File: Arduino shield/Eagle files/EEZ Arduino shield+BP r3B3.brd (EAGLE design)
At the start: 207 x 74 mm, 181 parts, among them IC1 TLC5925IDBQR, IC10 BC857BS, IC11 TLC555, IC12 SN74LVC2G08DCTR, IC13 TPS3705-33D, IC14 SN74LV1T34DBVR, IC15 SN74LVC2G02DCTR, IC2 Si8641EC-B-IS1, IC3 SI8651EC-B-IS1, IC4 SI8651EC-B-IS1, IC5 LD1117ADT33TR, IC6 Si8641EC-B-IS1, IC7 PCA21125, IC8 AT25256B, IC9 W5500, J1 BS-244DSM-R, J2 BS-244DSM-G, J3 BS-244DSM-B, J4 BS-244DSM-R, J5 BS-244DSM-B, Q1 IRLML2246TRPBF, Q2 IRLML2246TRPBF, Q3 IRLML2246TRPBF, Q4 IRLML2246TRPBF, Q5 2N7002, Q6 IRLML2246TRPBF, Q7 2N7002, Q8 2N7002, SW1 A101SYCQ04, SW2 1301.9316, X1 MC000006, X2 TSW-113-07-F-D, X3 MC000005, X4 TSW-113-07-F-D, X5 09185067324, X6 22-23-2021, X7 826629-8, X8 22-23-2041, X9 SSW-105-02-S-D, Y1 32,768kHz, Y2 25MHz

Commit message: Arduino Shield correction
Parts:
- C28, C32: device rcl:C0603 -> rcl:C0805
- moved C28 0.32 mm to (134.7, 21.9)
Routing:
- net CH1_VDD: vias 10 -> 9
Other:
- board text added: "1"
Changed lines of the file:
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@@
 <grid distance="2.5" unitdist="mil" unit="mil" style="lines" multiple="10" display="no" altdistance="5" altunitdist="mm" altunit="mm"/>
 <layers>
-<layer number="1" name="Top" color="4" fill="1" visible="no" active="yes"/>
+<layer number="1" name="Top" color="4" fill="1" visible="yes" active="yes"/>
 <layer number="2" name="Route2" color="1" fill="3" visible="no" active="no"/>
 <layer number="3" name="Route3" color="4" fill="3" visible="no" active="no"/>
@@
 <layer number="14" name="Route14" color="1" fill="6" visible="no" active="no"/>
 <layer number="15" name="Route15" color="4" fill="6" visible="no" active="no"/>
-<layer number="16" name="Bottom" color="1" fill="1" visible="no" active="yes"/>
-<layer number="17" name="Pads" color="14" fill="1" visible="no" active="yes"/>
-<layer number="18" name="Vias" color="14" fill="1" visible="no" active="yes"/>
-<layer number="19" name="Unrouted" color="6" fill="1" visible="no" active="yes"/>
-<layer number="20" name="Dimension" color="15" fill="1" visible="no" active="yes"/>
-<layer number="21" name="tPlace" color="7" fill="1" visible="no" active="yes"/>
-<layer number="22" name="bPlace" color="13" fill="1" visible="yes" active="yes"/>
-<layer number="23" name="tOrigins" color="15" fill="1" visible="no" active="yes"/>
+<layer number="16" name="Bottom" color="1" fill="1" visible="yes" active="yes"/>
+<layer number="17" name="Pads" color="14" fill="1" visible="yes" active="yes"/>
+<layer number="18" name="Vias" color="14" fill="1" visible="yes" active="yes"/>
+<layer number="19" name="Unrouted" color="6" fill="1" visible="yes" active="yes"/>
+<layer number="20" name="Dimension" color="15" fill="1" visible="yes" active="yes"/>
+<layer number="21" name="tPlace" color="7" fill="1" visible="yes" active="yes"/>
+<layer number="22" name="bPlace" color="13" fill="1" visible="no" active="yes"/>
+<layer number="23" name="tOrigins" color="15" fill="1" visible="yes" active="yes"/>
 <layer number="24" name="bOrigins" color="15" fill="1" visible="no" active="yes"/>
-<layer number="25" name="tNames" color="7" fill="1" visible="no" active="yes"/>
-<layer number="26" name="bNames" color="5" fill="1" visible="yes" active="yes"/>
+<layer number="25" name="tNames" color="7" fill="1" visible="yes" active="yes"/>
+<layer number="26" name="bNames" color="5" fill="1" visible="no" active="yes"/>
 <layer number="27" name="tValues" color="10" fill="1" visible="no" active="yes"/>
 <layer number="28" name="bValues" color="14" fill="1" visible="no" active="yes"/>
-<layer number="29" name="tStop" color="7" fill="3" visible="no" active="yes"/>
+<layer number="29" name="tStop" color="7" fill="3" visible="yes" active="yes"/>
 <layer number="30" name="bStop" color="7" fill="6" visible="no" active="yes"/>
 <layer number="31" name="tCream" color="7" fill="4" visible="no" active="yes"/>
@@
 <layer number="37" name="tTest" color="7" fill="1" visible="no" active="yes"/>
 <layer number="38" name="bTest" color="7" fill="1" visible="no" active="yes"/>
-<layer number="39" name="tKeepout" color="15" fill="1" visible="no" active="yes"/>
+<layer number="39" name="tKeepout" color="15" fill="1" visible="yes" active="yes"/>
 <layer number="40" name="bKeepout" color="5" fill="1" visible="no" active="yes"/>
 <layer number="41" name="tRestrict" color="4" fill="10" visible="no" active="yes"/>
@@
 <text x="147.193" y="32.0675" size="1.016" layer="125" ratio="10" rot="R90">C26</text>
 <text x="103.886" y="15.621" size="1.016" layer="125" ratio="10" rot="R180">C27</text>
-<text x="132.842" y="22.4155" size="1.016" layer="125" ratio="10" rot="R180">C28</text>
+<text x="132.7785" y="22.4155" size="1.016" layer="125" ratio="10" rot="R180">C28</text>
 <text x="111.76" y="20.32" size="1.016" layer="125" ratio="10" rot="R270">C29</text>
 <text x="103.886" y="17.5895" size="1.016" layer="125" ratio="10" rot="R180">C30</text>
@@
 <text x="19.3460125" y="31.829503125" size="1.27" layer="125" ratio="10">ZD4</text>
 <text x="75.438" y="70.4215" size="1.016" layer="125" ratio="10">ZD5</text>
+<text x="143.637" y="10.8585" size="1.016" layer="21" ratio="10" rot="R90">1</text>
 </plain>
 <attributes>
@@
 <attribute name="VALUE" x="114.173" y="7.239" size="1.016" layer="27" ratio="10"/>
 </element>
-<element name="C28" library="rcl" package="C0603" value="18p" x="134.366" y="21.9075" smashed="yes">
-<attribute name="NAME" x="132.842" y="22.4155" size="1.016" layer="25" ratio="10" rot="R180"/>
-<attribute name="VALUE" x="133.096" y="21.5265" size="1.016" layer="27" ratio="10"/>
+<element name="C28" library="rcl" package="C0805" value="18p" x="134.6835" y="21.9075" smashed="yes">
+<attribute name="NAME" x="132.7785" y="22.4155" size="1.016" layer="25" ratio="10" rot="R180"/>
+<attribute name="VALUE" x="133.4135" y="21.5265" size="1.016" layer="27" ratio="10"/>
 </element>
-<element name="C32" library="rcl" package="C0603" value="18p" x="134.6835" y="6.5405" smashed="yes">
+<element name="C32" library="rcl" package="C0805" value="18p" x="134.6835" y="6.5405" smashed="yes">
 <attribute name="NAME" x="133.2865" y="4.318" size="1.016" layer="25" ratio="10"/>
 <attribute name="VALUE" x="136.017" y="6.985" size="1.016" layer="27" ratio="10" rot="R180"/>
@@
 <wire x1="196.596" y1="65.2145" x2="196.596" y2="63.754" width="0.6096" layer="1"/>
 <wire x1="196.596" y1="63.754" x2="196.5325" y2="63.6905" width="0.6096" layer="1"/>
-<wire x1="138.684" y1="11.2395" x2="139.319" y2="11.2395" width="0.6096" layer="16"/>
-<wire x1="139.319" y1="11.2395" x2="140.9065" y2="9.652" width="0.6096" layer="16"/>
-<wire x1="140.9065" y1="9.652" x2="143.4465" y2="9.652" width="0.6096" layer="16"/>
 <wire x1="143.4465" y1="9.652" x2="143.51" y2="9.7155" width="0.6096" layer="16"/>
 <wire x1="117.983" y1="26.0985" x2="120.015" y2="24.0665" width="1.016" layer="1"/>
@@
 <wire x1="186.309" y1="4.3815" x2="188.722" y2="6.7945" width="1.016" layer="1"/>
 <wire x1="188.722" y1="6.7945" x2="188.722" y2="7.366" width="1.016" layer="1"/>
+<wire x1="143.4465" y1="9.652" x2="140.2715" y2="9.652" width="0.4064" layer="16"/>
+<wire x1="140.2715" y1="9.652" x2="138.684" y2="11.2395" width="0.4064" layer="16"/>
 <wire x1="48.895" y1="60.2615" x2="48.8975" y2="60.259" width="0" layer="19" extent="1-1"/>
 <wire x1="25.4635" y1="67.818" x2="25.527" y2="67.818" width="0" layer="19" extent="1-1"/>
@@
 <via x="129.032" y="17.145" extent="1-16" drill="0.6" shape="octagon"/>
 <wire x1="127.1475" y1="16.736" x2="128.623" y2="16.736" width="0.254" layer="1"/>
-<wire x1="139.954" y1="12.5095" x2="141.224" y2="13.7795" width="0.254" layer="16"/>
 <wire x1="141.224" y1="13.7795" x2="145.034" y2="13.7795" width="0.254" layer="1"/>
 <via x="145.034" y="13.7795" extent="1-16" drill="0.6" shape="octagon"/>
@@
 <wire x1="111.76" y1="68.5165" x2="111.76" y2="66.1035" width="0.254" layer="1"/>
 <wire x1="111.76" y1="66.1035" x2="111.125" y2="65.4685" width="0.254" layer="1"/>
-<wire x1="139.954" y1="12.5095" x2="135.89" y2="12.5095" width="0.254" layer="16"/>
 <wire x1="135.89" y1="12.5095" x2="133.7945" y2="14.605" width="0.254" layer="16"/>
 <wire x1="133.7945" y1="14.605" x2="130.302" y2="14.605" width="0.254" layer="16"/>
 <wire x1="130.302" y1="14.605" x2="129.413" y2="15.494" width="0.254" layer="16"/>
+<wire x1="135.89" y1="12.5095" x2="139.5095" y2="12.5095" width="0.254" layer="16"/>
+<wire x1="139.5095" y1="12.5095" x2="140.7795" y2="13.7795" width="0.254" layer="16"/>
+<wire x1="140.7795" y1="13.7795" x2="141.224" y2="13.7795" width="0.254" layer="16"/>
 <wire x1="151.511" y1="54.102" x2="151.5" y2="54.14" width="0" layer="19" extent="16-16"/>
 <wire x1="105.3084" y1="52.1335" x2="105.283" y2="52.1335" width="0" layer="19" extent="1-1"/>
@@
 <wire x1="76.835" y1="54.1655" x2="76.835" y2="53.5432" width="0.254" layer="1"/>
 <wire x1="76.835" y1="53.5432" x2="76.7842" y2="53.4924" width="0.254" layer="1"/>
-<via x="76.835" y="56.515" extent="1-16" drill="0.6" shape="octagon"/>
-<wire x1="76.835" y1="56.515" x2="76.835" y2="54.1655" width="0.254" layer="16"/>
+<wire x1="76.835" y1="56.7055" x2="76.835" y2="54.1655" width="0.254" layer="1"/>
 <wire x1="86.6902" y1="51.1175" x2="89.2175" y2="51.1175" width="0.4064" layer="1"/>
 <wire x1="89.2175" y1="51.1175" x2="89.2175" y2="54.9275" width="0.4064" layer="16"/>
@@
 <wire x1="101.6635" y1="38.7985" x2="100.584" y2="39.878" width="0.4064" layer="16"/>
 <wire x1="100.2665" y1="40.1955" x2="100.584" y2="39.878" width="0.4064" layer="1"/>
-<wire x1="76.835" y1="56.515" x2="76.835" y2="56.7055" width="0.254" layer="1"/>
 <wire x1="89.2175" y1="54.9275" x2="89.154" y2="54.9275" width="0" layer="19" extent="1-16"/>
 <wire x1="84.162" y1="50.927" x2="84.074" y2="50.927" width="0" layer="19" extent="1-1"/>
@@
 <wire x1="131.7585" y1="15.236" x2="134.0485" y2="17.526" width="0.254" layer="1"/>
 <wire x1="133.7945" y1="18.474" x2="134.0485" y2="17.526" width="0.254" layer="1"/>
-<wire x1="133.516" y1="21.9075" x2="133.516" y2="18.835" width="0.254" layer="1"/>
-<wire x1="133.516" y1="18.835" x2="133.731" y2="18.415" width="0.254" layer="1"/>
-<wire x1="133.7945" y1="18.474" x2="133.731" y2="18.415" width="0" layer="19" extent="1-1"/>
+<wire x1="133.7945" y1="18.474" x2="133.731" y2="18.474" width="0.254" layer="1"/>
+<wire x1="133.731" y1="18.474" x2="133.731" y2="21.9075" width="0.254" layer="1"/>
+<wire x1="133.731" y1="21.9075" x2="133.7335" y2="21.9075" width="0" layer="19" extent="1-1"/>
 </signal>
 <signal name="ETH_OUT-">
@@
 <wire x1="133.7945" y1="9.974" x2="133.7945" y2="12.7635" width="0.254" layer="1"/>
 <wire x1="133.7945" y1="12.7635" x2="131.826" y2="14.732" width="0.254" layer="1"/>
-<wire x1="133.8335" y1="6.5405" x2="133.8335" y2="9.935" width="0.254" layer="1"/>
+<wire x1="133.7335" y1="6.5405" x2="133.8335" y2="9.935" width="0.254" layer="1"/>
 <wire x1="133.8335" y1="9.935" x2="133.7945" y2="9.974" width="0.254" layer="1"/>
 <wire x1="131.826" y1="14.732" x2="131.822" y2="14.736" width="0" layer="19" extent="1-1"/>

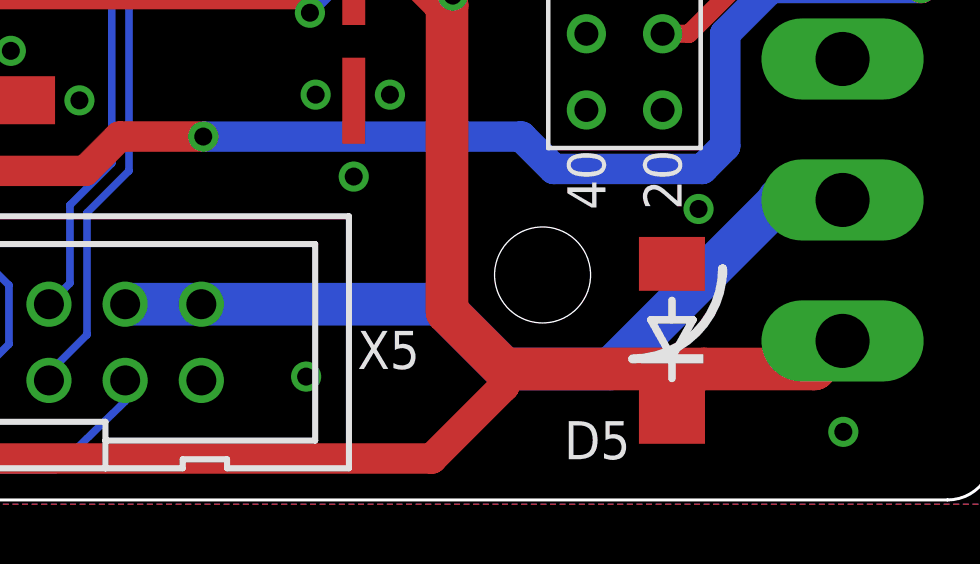
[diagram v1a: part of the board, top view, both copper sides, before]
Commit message: Arduino shield D5 PCB layout, BOM corrections
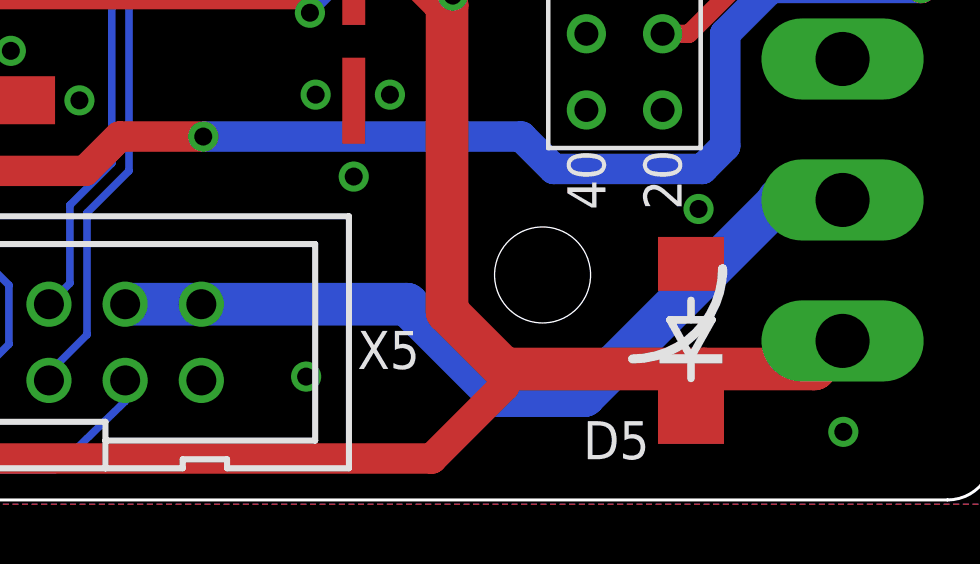
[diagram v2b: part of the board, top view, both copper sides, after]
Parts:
- moved D5 0.63 mm to (194.9, 8.32)
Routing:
- net N$1: track 27.2 -> 27.9 mm
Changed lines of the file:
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@@
 <text x="75.438" y="70.4215" size="1.016" layer="125" ratio="10">ZD5</text>
 <text x="143.637" y="10.8585" size="1.016" layer="21" ratio="10" rot="R90">1</text>
+<circle x="105" y="69.5" radius="2.75" width="0.1" layer="51"/>
+<circle x="105" y="10.5" radius="2.75" width="0.1" layer="51"/>
+<circle x="190" y="10.5" radius="2.75" width="0.1" layer="51"/>
+<circle x="190" y="69.5" radius="2.75" width="0.1" layer="51"/>
 </plain>
 <attributes>
@@
 <attribute name="VALUE" x="36.8935" y="53.0225" size="1.016" layer="27" ratio="10"/>
 </element>
-<element name="D5" library="MyLib6" package="DO214AA" value="SMBJ5.0A-TR" x="194.312" y="8.3185" smashed="yes" rot="R90">
-<attribute name="NAME" x="190.7195" y="4.357" size="1.27" layer="25" ratio="10"/>
-<attribute name="VALUE" x="194.7955" y="2.44" size="1.016" layer="27" ratio="10" rot="R90"/>
+<element name="D5" library="MyLib6" package="DO214AA" value="SMBJ5.0A-TR" x="194.947" y="8.3185" smashed="yes" rot="R90">
+<attribute name="NAME" x="191.3545" y="4.357" size="1.27" layer="25" ratio="10"/>
+<attribute name="VALUE" x="195.4305" y="2.44" size="1.016" layer="27" ratio="10" rot="R90"/>
 </element>
 <element name="R1" library="rcl" package="R0805" value="4K7" x="93.218" y="15.8115" smashed="yes">
@@
 <wire x1="177.9905" y1="68.0085" x2="176.911" y2="66.929" width="0.6096" layer="1"/>
 <contactref element="D5" pad="C"/>
-<wire x1="194.312" y1="5.7685" x2="195.2645" y2="7.241" width="0.254" layer="1"/>
+<wire x1="194.947" y1="5.7685" x2="195.2645" y2="7.241" width="0.254" layer="1"/>
 <wire x1="195.2645" y1="7.241" x2="195.3895" y2="7.366" width="0.254" layer="1"/>
 <contactref element="LED_O1" pad="A"/>
@@
 <signal name="N$1">
 <contactref element="SW1" pad="2"/>
-<wire x1="188.722" y1="7.366" x2="192.278" y2="7.366" width="1.4224" layer="16"/>
-<wire x1="192.278" y1="7.366" x2="197.866" y2="12.954" width="1.4224" layer="16"/>
+<wire x1="191.389" y1="6.477" x2="197.866" y2="12.954" width="1.4224" layer="16"/>
 <wire x1="197.866" y1="12.954" x2="197.866" y2="13.0175" width="1.4224" layer="16"/>
 <wire x1="197.866" y1="12.954" x2="199.954" y2="12.954" width="1.4224" layer="16"/>
@@
 <contactref element="X5" pad="10"/>
 <wire x1="178.6255" y1="9.525" x2="176.0855" y2="9.525" width="1.4224" layer="16"/>
-<wire x1="178.6255" y1="9.525" x2="186.563" y2="9.525" width="1.4224" layer="16"/>
-<wire x1="186.563" y1="9.525" x2="188.722" y2="7.366" width="1.4224" layer="16"/>
+<wire x1="191.389" y1="6.477" x2="188.5315" y2="6.477" width="1.4224" layer="16"/>
+<wire x1="188.5315" y1="6.477" x2="185.4835" y2="9.525" width="1.4224" layer="16"/>
+<wire x1="185.4835" y1="9.525" x2="178.6255" y2="9.525" width="1.4224" layer="16"/>
 </signal>
 <signal name="NTC1">
@@
 </signal>
 </signals>
+<errors>
+</errors>
 </board>
 </drawing>

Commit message: Arduino shield renumbering
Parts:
- removed C1, C6: 470n/100V, rcl:C1812
- removed C10, C11, C12, C13, C14, C15, C18, C19, C20, C21, C23, C25, C26, C33, C34, C35, C36, C37, C38, C39, C40, C44, C46, C47, C48, C50, C53: 100n, rcl:C0603
- removed C16: 47u, MyLib6:PANASONIC_C
- removed C17: 10u, MyLib6:PANASONIC_C
- removed C2, C5, C7, C9: 10n, rcl:C1206
- removed C22, C4: 10u, rcl:C1206
- removed C24: EECS5R5H105, EEZ_Lib1:SG-R20MM
- removed C27: 22n, rcl:C0805
- removed C28, C32: 18p, rcl:C0805
- removed C29, C31: 6n8, rcl:C0603
- removed C3, C8: UPW1J150MED, MyLib6:CAPAE660X610N_COMBO2
- removed C30, C43, C51, C52: 10n, rcl:C0805
- removed C41: 10u, EEZ_Lib1:EC1206
- removed C42: 4u7, EEZ_Lib1:EC1206
- removed C45, C49: 47n, rcl:C0805
- removed D1, D2, D3, D4, D6: BAS316, diode:SOD323-W
- removed D5: SMBJ5.0A-TR, MyLib6:DO214AA
- removed D7: BAT54S, diode:SOT23
- removed D8: SKL16, diode:DO214AC
- removed EEZ_SIGNATURE: SIGNATURESMALL, MyLib6:SIGNATURE_5MM
- removed FB: 60R@100MHz, EEZ_Lib1:BEAD0603
- removed IC1: TLC5925IDBQR, MyLib6:SOP63P600X175-24N
- removed IC10: BC857BS, MyLib6:SOT65P210X110-6N
- removed IC11: TLC555, MyLib6:SOIC127P600X175-8N
- removed IC12: SN74LVC2G08DCTR, EEZ_Lib1:SOP65P400X130-8N
- removed IC13: TPS3705-33D, EEZ_Lib1:SOIC127P600X175-8N
- removed IC14: SN74LV1T34DBVR, EEZ_Lib1:SOT95P280X145-5N
- removed IC15: SN74LVC2G02DCTR, EEZ_Lib1:SOP65P400X130-8N
- removed IC2, IC6: Si8641EC-B-IS1, EEZ_Lib1:SOIC-16
- removed IC3, IC4: SI8651EC-B-IS1, EEZ_Lib1:SOIC-16
- removed IC5: LD1117ADT33TR, v-reg:DPACK
- removed IC7: PCA21125, MyLib6:SOP65P640X120-14N
- removed IC8: AT25256B, MyLib6:SOIC127P600X175-8N
- removed IC9: W5500, EEZ_Lib1:TQFP48-7X7
- removed JP1: 826926-2, jumper:JP1
- removed JP2: 0R-JUMPA, jump-0r-smd:A0R-JMP
- removed OK1: HCPL-181, EEZ_Lib1:HCPL-181
- removed Q1, Q2, Q3, Q4, Q6: IRLML2246TRPBF, MyLib6:SOT95P237X112-3N
- removed Q5, Q7, Q8: 2N7002, MyLib6:SOT103P240X110-3N
- removed R1, R11, R12, R2, R35, R37, R6, R8: 4K7, rcl:R0805
- removed R10, R21, R4: 100K, rcl:R0805
- removed R13, R15, R16, R17: 49R9, rcl:R0805
- removed R14, R20, R24, R36, R38: 10K, rcl:R0805
- removed R18: 10R, rcl:R0805
- removed R19: 12K4, rcl:R0805
- removed R22, R23, R25, R9: 180R, rcl:R0805
- removed R26, R27, R5: 1K5, rcl:R0805
- removed R28, R29: 30K, rcl:R0805
- removed R3, R7: 1R, rcl:R0805
- removed R30: 100R, rcl:R0805
- removed R31: 0R, rcl:R0805
- removed R32: 10K, resistor:R1206
- removed R33, R34: 1K, rcl:R0805
- removed SH1: (no value), EEZ_Lib1:SHORT_NOHOLE
- removed TP1, TP2: (no value), EEZ_Lib1:TP_1.1MM
- removed U$2: (no value), olimex_logo1:RECYCLE_BIN1/8
- removed U$3: (no value), olimex_logo1:PB_SMALL
- removed U$4: (no value), olimex_logo1:ESD_SYMBOL
- removed X1: MC000006, EEZ_Lib1:MC000006_MIRROR
- removed X2, X4: TSW-113-07-F-D, EEZ_Lib1:TSW-113-07-F-D
- removed X3: MC000005, EEZ_Lib1:MC000005_MIRROR
- removed X5: 09185067324, EEZ_Lib1:IDC-10PIN
- removed X6: 22-23-2021, con-molex:22-23-2021
- removed X7: 826629-8, con-samtec:SSW-108-02-S-S
- removed X8: 22-23-2041, con-molex:22-23-2041
- removed X9: SSW-105-02-S-D, con-samtec:SSW-105-02-S-D
- removed ZD1, ZD2: P4SMAJ60A, EEZ_Lib1:DO214AC
- removed ZD3, ZD4: SMAJ18A, EEZ_Lib1:DO214AC
- removed ZD5: 4V3, EEZ_Lib1:MINIMELF
- added C105, C110: 470n/100V, rcl:C1812
- added C106, C109, C111, C113: 10n, rcl:C1206
- added C107, C112: UPW1J150MED, MyLib6:CAPAE660X610N_COMBO2
- added C108, C126: 10u, rcl:C1206
- added C114, C115, C116, C117, C118, C119, C122, C123, C124, C125, C127, C129, C130, C137, C138, C139, C140, C141, C142, C143, C144, C148, C150, C151, C152, C154, C157: 100n, rcl:C0603
- added C120: 47u, MyLib6:PANASONIC_C
- added C121: 10u, MyLib6:PANASONIC_C
- added C128: EECS5R5H105, EEZ_Lib1:SG-R20MM
- added C131: 22n, rcl:C0805
- added C132, C136: 18p, rcl:C0805
- added C133, C135: 6n8, rcl:C0603
- added C134, C147, C155, C156: 10n, rcl:C0805
- added C145: 10u, EEZ_Lib1:EC1206
- added C146: 4u7, EEZ_Lib1:EC1206
- added C149, C153: 47n, rcl:C0805
- added D22, D23, D24, D25, D27: BAS316, diode:SOD323-W
- added D26: SMBJ5.0A-TR, MyLib6:DO214AA
- added D28: BAT54S, diode:SOT23
- added D29: SKL16, EEZ_Lib1:SOD123
- added EEZ_SIGNATURE2: SIGNATURESMALL, MyLib6:SIGNATURE_5MM
- added FB8: 60R@100MHz, EEZ_Lib1:BEAD0603
- added IC21: TLC5925IDBQR, MyLib6:SOP63P600X175-24N
- added IC22, IC26: Si8641EC-B-IS1, EEZ_Lib1:SOIC-16
- added IC23, IC24: SI8651EC-B-IS1, EEZ_Lib1:SOIC-16
- added IC25: LD1117ADT33TR, v-reg:DPACK
- added IC27: PCA21125, MyLib6:SOP65P640X120-14N
- added IC28: AT25256B, MyLib6:SOIC127P600X175-8N
- added IC29: W5500, EEZ_Lib1:TQFP48-7X7
- added IC30: BC857BS, MyLib6:SOT65P210X110-6N
- added IC31: TLC555, MyLib6:SOIC127P600X175-8N
- added IC32: SN74LVC2G08DCTR, EEZ_Lib1:SOP65P400X130-8N
- added IC33: TPS3705-33D, EEZ_Lib1:SOIC127P600X175-8N
- added IC34: SN74LV1T34DBVR, EEZ_Lib1:SOT95P280X145-5N
- added IC35: SN74LVC2G02DCTR, EEZ_Lib1:SOP65P400X130-8N
- added JP6, JP7: 0R-JUMPA, jump-0r-smd:A0R-JMP
- added OK3: HCPL-181, EEZ_Lib1:HCPL-181
- added Q23, Q24, Q25, Q26, Q28: IRLML2246TRPBF, MyLib6:SOT95P237X112-3N
- added Q27, Q29, Q30: 2N7002, MyLib6:SOT103P240X110-3N
- added R122, R123, R127, R129, R132, R133, R156, R158: 4K7, rcl:R0805
- added R124, R128: 1R, rcl:R0805
- added R125, R131, R142: 100K, rcl:R0805
- added R126, R147, R148: 1K5, rcl:R0805
- added R130, R143, R144, R146: 180R, rcl:R0805
- added R134, R136, R137, R138: 49R9, rcl:R0805
- added R135, R141, R145, R157, R159: 10K, rcl:R0805
- added R139: 10R, rcl:R0805
- added R140: 12K4, rcl:R0805
- added R149, R150: 30K, rcl:R0805
- added R151: 100R, rcl:R0805
- added R152: 0R, rcl:R0805
- added R153: 10K, resistor:R1206
- added R154, R155: 1K, rcl:R0805
- added SH3: (no value), EEZ_Lib1:SHORT_NOHOLE
- added TP3, TP4: (no value), EEZ_Lib1:TP_1.1MM
- added U$7: (no value), olimex_logo1:ESD_SYMBOL
- added U$8: (no value), olimex_logo1:RECYCLE_BIN1/8
- added U$9: (no value), olimex_logo1:PB_SMALL
- added X12: MC000006, EEZ_Lib1:MC000006_MIRROR
- added X13, X15: TSW-113-07-F-D, EEZ_Lib1:TSW-113-07-F-D
- added X14: MC000005, EEZ_Lib1:MC000005_MIRROR
- added X16: 09185067324, EEZ_Lib1:IDC-10PIN
- added X17: 22-23-2021, con-molex:22-23-2021
- added X18: 826629-8, con-samtec:SSW-108-02-S-S
- added X19: 22-23-2041, con-molex:22-23-2041
- added X20: SSW-105-02-S-D, con-samtec:SSW-105-02-S-D
- added ZD10, ZD11: SMAJ18A, EEZ_Lib1:DO214AC
- added ZD12: 4V3, EEZ_Lib1:MINIMELF
- added ZD8, ZD9: P4SMAJ60A, EEZ_Lib1:DO214AC
- JP3: value 0R-JUMPA -> 826926-2; device jump-0r-smd:A0R-JMP -> jumper:JP1
- LED_CC1, LED_CC2, LED_CV1, LED_CV2, LED_O1, LED_O2, LED_PROG1, LED_PROG2, LED_PWR, LED_S1, LED_S2, LED_SP: device led:CHIPLED_0805 -> EEZ_Lib1:LED_0805
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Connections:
- removed net N$1: SW1.2, X5.10, X5.8
- removed net N$10: JP2.2, LCD1.2
- removed net N$11: IC9.43, RN2.3
- removed net N$12: IC9.44, RN2.2
- removed net N$13: Q6.3, R18.1
- removed net N$14: IC9.45, RN2.1
- removed net N$15: IC9.42, RN2.4
- removed net N$16: JP4.2, LCD1.31
- removed net N$17: IC10.6, IC11.7, R27.1
- removed net N$18: JP3.2, LCD1.29
- removed net N$19: C45.2, IC11.2, IC11.6, R27.2
- removed net N$2: JP5.2, LCD1.33
- removed net N$20: D7.2, R30.1, ZD5.C
- removed net N$21: R35.2, R36.2, X8.2
- removed net N$22: C24.1, R9.1
- removed net N$23: IC9.38, RN1.4
- removed net N$24: IC7.1, Y1.2
- removed net N$25: IC7.2, Y1.1
- removed net N$26: D7.3, R32.2, R33.2
- removed net N$27: IC14.2, R33.1
- removed net N$28: IC9.39, RN1.3
- removed net N$29: IC9.41, RN1.1
- removed net N$3: OK1.1, R25.2
- removed net N$30: IC14.4, R34.2
- removed net N$31: C1.2, R3.2
- removed net N$32: C6.2, R7.2
- removed net N$33: D8.C, R30.2
- removed net N$34: R32.1, X1.2, X1.2.1
- removed net N$35: D8.A, FB.P$2
- removed net N$36: IC9.40, RN1.2
- removed net N$37: IC1.16, LED_PROG2.C
- removed net N$38: C34.2, Q6.1, R20.2, R21.1
- removed net N$4: C32.1, IC9.30, Y2.2
- removed net N$40: R23.2, X7.1
- removed net N$41: R22.2, X7.2
- removed net N$42: IC13.6, R31.1
- removed net N$43: IC12.3, Q7.1, R28.1
- removed net N$44: IC12.7, Q8.1, R29.1
- removed net N$45: IC9.10, R19.2
- removed net N$47: R37.2, R38.2, X8.3
- removed net N$5: IC9.23, R24.2
- removed net N$6: C29.2, IC9.5
- removed net N$7: C31.2, IC9.6
- removed net N$71: Q5.3, SG1.-, SG1.-B
- removed net N$8: D1.C, K_S1.1, Q1.3
- removed net N$9: D4.C, K_S2.1, Q4.3
- removed net N$97 (its old number): C28.1, IC9.31, Y2.1
- new net N$100: SW1.2, X16.10, X16.8
- new net N$101: Q27.3, SG1.-, SG1.-B
- new net N$102: JP4.2, LCD1.2
- new net N$103: Q28.3, R139.1
- new net N$104: JP7.2, LCD1.33
- new net N$105: JP5.2, LCD1.29
- new net N$106: JP6.2, LCD1.31
- new net N$107: C128.1, R130.1
- new net N$108: IC29.23, R145.2
- new net N$110: IC29.10, R140.2
- new net N$111: C132.1, IC29.31, Y2.1
- new net N$112: C136.1, IC29.30, Y2.2
- new net N$113: C133.2, IC29.5
- new net N$115: C135.2, IC29.6
- new net N$116: R144.2, X18.1
- new net N$118: R143.2, X18.2
- new net N$119: IC29.43, RN2.3
- new net N$120: IC29.44, RN2.2
- new net N$121: IC29.45, RN2.1
- new net N$122: IC29.42, RN2.4
- new net N$123: IC29.38, RN1.4
- new net N$126: IC29.39, RN1.3
- new net N$127: IC29.41, RN1.1
- new net N$130: IC29.40, RN1.2
- new net N$132: C138.2, Q28.1, R141.2, R142.1
- new net N$133: IC27.1, Y1.2
- new net N$134: IC27.2, Y1.1
- new net N$136: C149.2, IC31.2, IC31.6, R148.2
- new net N$137: IC30.6, IC31.7, R148.1
- new net N$138: OK3.1, R146.2
- new net N$139: D28.3, R153.2, R154.2
- new net N$140: IC34.2, R154.1
- new net N$141: IC34.4, R155.2
- new net N$142: R153.1, X12.2, X12.2.1
- new net N$144: D28.2, R151.1, ZD12.C
- new net N$148: D29.C, R151.2
- new net N$149: D29.A, FB8.P$2
- new net N$151: IC33.6, R152.1
- new net N$152: IC32.3, Q29.1, R149.1
- new net N$154: IC32.7, Q30.1, R150.1
- new net N$157: R156.2, R157.2, X19.2
- new net N$159: R158.2, R159.2, X19.3
- new net N$92: D22.C, K_S1.1, Q23.3
- new net N$93: D25.C, K_S2.1, Q26.3
- new net N$94: C105.2, R124.2
- new net N$95: C110.2, R128.2
- new net N$96: IC21.16, LED_PROG2.C
- net !ADC1_SELECT: now also IC23.4; no longer IC3.4
- net !ADC2_SELECT: now also IC26.4; no longer IC6.4
- net !BP_OE: now also IC21.21; no longer IC1.21
- net !BP_OUT0: now also IC21.5; no longer IC1.5
- net !BP_OUT1: now also IC21.6, Q23.1, R122.1; no longer IC1.6, Q1.1, R1.1
- net !BP_OUT10: now also IC21.15; no longer IC1.15
- net !BP_OUT12: now also IC21.17; no longer IC1.17
- net !BP_OUT13: now also IC21.18; no longer IC1.18
- net !BP_OUT14: now also IC21.19, Q26.1, R127.1; no longer IC1.19, Q4.1, R6.1
- net !BP_OUT15: now also IC21.20; no longer IC1.20
- net !BP_OUT2: now also IC21.7; no longer IC1.7
- net !BP_OUT3: now also IC21.8; no longer IC1.8
- net !BP_OUT4: now also IC21.9; no longer IC1.9
- net !BP_OUT5: now also IC21.10; no longer IC1.10
- net !BP_OUT6: now also IC21.11; no longer IC1.11
- net !BP_OUT7: now also IC21.12; no longer IC1.12
- net !BP_OUT8: now also IC21.13, Q25.1, R123.1; no longer IC1.13, Q3.1, R2.1
- net !BP_OUT9: now also IC21.14, Q24.1, R125.1; no longer IC1.14, Q2.1, R4.1
- net !CH1_ADC: now also IC23.13, X13.6; no longer IC3.13, X2.6
- net !CH1_DAC: now also IC22.12, X13.4; no longer IC2.12, X2.4
- net !CH1_EXPANDER: now also IC22.13, X13.3; no longer IC2.13, X2.3
- net !CH1_INT: now also IC23.11, X13.8; no longer IC3.11, X2.8
- net !CH1_RESET: now also IC23.14, X13.5; no longer IC3.14, X2.5
- net !CH2_ADC: now also IC26.13, X15.6; no longer IC6.13, X4.6
- net !CH2_DAC: now also IC24.12, X15.4; no longer IC4.12, X4.4
- net !CH2_EXPANDER: now also IC24.13, X15.3; no longer IC4.13, X4.3
- net !CH2_INT: now also IC24.11, X15.8; no longer IC4.11, X4.8
- net !CH2_RESET: now also IC26.14, X15.5; no longer IC6.14, X4.5
- net !CONVEND1: now also IC23.6; no longer IC3.6
- net !CONVEND2: now also IC24.6; no longer IC4.6
- net !DAC1_SELECT: now also IC22.5; no longer IC2.5
- net !DAC2_SELECT: now also IC24.5; no longer IC4.5
- net !EEPROM_SELECT: now also IC28.1; no longer IC8.1
- net !ETH_IRQ: now also IC29.36, X20.8; no longer IC9.36, X9.8
- net !ETH_SELECT: now also IC29.32, X20.7; no longer IC9.32, X9.7
- net !IO_EXPANDER1: now also IC22.4; no longer IC2.4
- net !IO_EXPANDER2: now also IC24.4; no longer IC4.4
- net !MR: now also C153.2, IC33.1; no longer C49.2, IC13.1
- net !PWD_RST: now also JP3.1; no longer JP1.1
- net !RESET: now also IC23.3, IC26.3, IC29.37, IC32.2, IC32.5, IC33.7, X20.6; no longer IC12.2, IC12.5, IC13.7, IC3.3, IC6.3, IC9.37, X9.6
- net !RTC_IRQ: now also IC27.5; no longer IC7.5
- net +3V3: now also C108.1, C115.1, C116.1, C118.1, C121.1, C123.1, C127.1, C131.1, C137.2, C139.1, C140.1, C141.1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; no longer C11.1, C12.1, C15.1, C17.1, C19.1, C23.1, C27.1, C33.2, C35.1, C36.1, C37.1, C38.1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
- net +5V: now also C120.1, C126.2, D26.C, FB8.P$1, IC25.3, JP4.1, Q23.2, Q24.2, Q25.2, Q26.2, R122.2, R123.2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; no longer C16.1, C22.2, D5.C, FB.P$1, IC5.3, JP2.1, Q1.2, Q2.2, Q3.2, Q4.2, R1.2, R2.2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
- net 1V2O: now also C147.2, IC29.22; no longer C43.2, IC9.22
- net AUX1_USET_IN: now also X12.8, X12.8.1, X13.11, ZD10.C; no longer X1.8, X1.8.1, X2.11, ZD3.C
- net AUX2_USET_IN: now also X14.6, X14.6.1, X15.11, ZD11.C; no longer X3.6, X3.6.1, X4.11, ZD4.C
- net BATT_NTC: now also OK3.4, R147.2; no longer OK1.4, R26.2
- net BP_SELECT: now also IC21.4; no longer IC1.4
- net BUZZER: now also Q27.1, R131.2; no longer Q5.1, R10.2
- net CH1_GND: now also C114.2, C117.2, C148.2, C149.1, IC22.15, IC22.9, IC23.9, IC31.1, OK3.2, X12.6, X12.6.1, X13.10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; no longer C10.2, C13.2, C44.2, C45.1, IC11.1, IC2.15, IC2.9, IC3.9, OK1.2, X1.6, X1.6.1, X2.10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
- net CH1_MISO: now also IC22.11, X13.9; no longer IC2.11, X2.9
- net CH1_MOSI: now also IC22.14, X13.1; no longer IC2.14, X2.1
- net CH1_SCLK: now also IC23.12, X13.7; no longer IC3.12, X2.7
- net CH1_SYNC: now also IC23.15, X13.16; no longer IC3.15, X2.16
- net CH1_VDD: now also C114.1, C117.1, C148.1, IC22.10, IC22.16, IC23.10, IC23.16, IC30.1, IC30.4, IC31.4, IC31.8, X13.2; no longer C10.1, C13.1, C44.1, IC10.1, IC10.4, IC11.4, IC11.8, IC2.10, IC2.16, IC3.10, IC3.16, X2.2
- net CH2_GND: now also C119.2, C122.2, IC24.9, IC26.15, IC26.9, X14.5, X14.5.1, X15.10, X15.12, X15.14, ZD11.A; no longer C14.2, C18.2, IC4.9, IC6.15, IC6.9, X3.5, X3.5.1, X4.10, X4.12, X4.14, ZD4.A
- net CH2_MISO: now also IC26.11, X15.9; no longer IC6.11, X4.9
- net CH2_MOSI: now also IC24.14, X15.1; no longer IC4.14, X4.1
- net CH2_SCLK: now also IC26.12, X15.7; no longer IC6.12, X4.7
- net CH2_SYNC: now also IC24.15, X15.16; no longer IC4.15, X4.16
- net CH2_VDD: now also C119.1, C122.1, IC24.10, IC24.16, IC26.10, IC26.16, X15.2; no longer C14.1, C18.1, IC4.10, IC4.16, IC6.10, IC6.16, X4.2
- net EARTH: now also C106.2, C109.1, C111.2, C113.1, C131.2, C134.2, X12.3, X12.3.1, X14.1, X14.1.1, X18.3; no longer C2.2, C27.2, C30.2, C5.1, C7.2, C9.1, X1.3, X1.3.1, X3.1, X3.1.1, X7.3
- net ENC_A: now also C155.2, MCU.A8, R157.1; no longer C51.2, MCU.A14, R36.1
- net ENC_B: now also C156.1, MCU.A9, R159.1; no longer C52.1, MCU.A15, R38.1
- net ETH_ACTLED: now also IC29.27, R143.1; no longer IC9.27, R22.1
- net ETH_IN+: now also C135.1, R138.1, X18.4; no longer C31.1, R17.1, X7.4
- net ETH_IN-: now also C133.1, R137.2, X18.5; no longer C29.1, R16.2, X7.5
- net ETH_LINKLED: now also IC29.25, R144.1; no longer IC9.25, R23.1
- net ETH_OUT+: now also IC29.2, R136.1, X18.6; no longer IC9.2, R15.1, X7.6
- net ETH_OUT-: now also IC29.1, R134.2, X18.7; no longer IC9.1, R13.2, X7.7
- net EXT_TRIG: now also R155.1; no longer R34.1
- net FAN_PWM: now also X16.6; no longer X5.6
- net FAN_SENSE: now also X16.5; no longer X5.5
- net GND: now also C108.2, C115.2, C116.2, C118.2, C120.2, C121.2, C123.2, C124.1, C125.1, C126.1, C127.2, C128.2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; no longer C11.2, C12.2, C15.2, C16.2, C17.2, C19.2, C20.1, C21.1, C22.1, C23.2, C24.2, C25.1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
- net GNDA: now also C146.-, IC29.14, IC29.16, IC29.19, IC29.3, IC29.48, IC29.9, R140.1, SH3.P$2; no longer C42.-, IC9.14, IC9.16, IC9.19, IC9.3, IC9.48, IC9.9, R19.1, SH1.P$2
- net ISOLATOR1_EN: now also IC22.7; no longer IC2.7
- net ISOLATOR2_EN: now also IC26.7; no longer IC6.7
- net LCD_BRIGHTNESS: now also R141.1; no longer R20.1
- net LCD_RD: now also R135.1; no longer R14.1
- net LED_A: now also R139.2; no longer R18.2
- net MISO: now also IC22.6, IC26.6, IC27.8, IC28.2, IC29.34, JP7.1, X20.3; no longer IC2.6, IC6.6, IC7.8, IC8.2, IC9.34, JP5.1, X9.3
- net MOSI: now also IC21.2, IC22.3, IC24.3, IC27.9, IC28.5, IC29.35, JP6.1, X20.5; no longer IC1.2, IC2.3, IC4.3, IC7.9, IC8.5, IC9.35, JP4.1, X9.5
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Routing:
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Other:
- board text added: "C105"
- board text added: "C106"
- board text added: "C107"
- board text added: "C108"
- board text added: "C109"
- board text added: "C110"
- board text added: "C111"
- board text added: "C112"
- board text added: "C113"
- board text added: "C114"
- board text added: "C115"
- board text added: "C116"
- board text added: "C117"
- board text added: "C118"
- board text added: "C119"
- board text added: "C120"
- board text added: "C121"
- board text added: "C122"
- board text added: "C123"
- board text added: "C124"
- board text added: "C125"
- board text added: "C126"
- board text added: "C127"
- board text added: "C128"
- board text added: "C129"
- board text added: "C130"
- board text added: "C131"
- board text added: "C132"
- board text added: "C133"
- board text added: "C134"
- board text added: "C135"
- board text added: "C136"
- board text added: "C137"
- board text added: "C138"
- board text added: "C139"
- board text added: "C140"
- board text added: "C141"
- board text added: "C142"
- board text added: "C143"
- board text added: "C144"
- board text added: "C145"
- board text added: "C146"
- board text added: "C147"
- board text added: "C148"
- board text added: "C149"
- board text added: "C150"
- board text added: "C151"
- board text added: "C152"
- board text added: "C153"
- board text added: "C154"
- board text added: "C155"
- board text added: "C156"
- board text added: "C157"
- board text added: "Ch#1 control X12"
- board text added: "Ch#2 control X14"
- board text added: "D22"
- board text added: "D23"
- board text added: "D24"
- board text added: "D25"
- board text added: "D26"
- board text added: "D27"
- board text added: "D28"
- board text added: "D29"
- board text added: "Encoder X19"
- board text added: "Ethernet module X20"
- board text added: "FB8"
- board text added: "IC21"
- board text added: "IC22"
- board text added: "IC23"
- board text added: "IC24"
- board text added: "IC25"
- board text added: "IC26"
- board text added: "IC27"
- board text added: "IC28"
- board text added: "IC29"
- board text added: "IC30"
- board text added: "IC31"
- board text added: "IC32"
- board text added: "IC33"
- board text added: "IC34"
- board text added: "IC35"
- board text added: "JP6"
- board text added: "JP7"
- board text added: "OK3"
- board text added: "Power X16"
- board text added: "Power module X13,X14"
- board text added: "Q23"
- board text added: "Q24"
- board text added: "Q25"
- board text added: "Q26"
- board text added: "Q27"
- board text added: "Q28"
- board text added: "Q29"
- board text added: "Q30"
- board text added: "R122"
- board text added: "R123"
- board text added: "R124"
- board text added: "R125"
- board text added: "R126"
- board text added: "R127"
- board text added: "R128"
- board text added: "R129"
- board text added: "R130"
- board text added: "R131"
- board text added: "R132"
- board text added: "R133"
- board text added: "R134"
- board text added: "R135"
- board text added: "R136"
- board text added: "R137"
- board text added: "R138"
- board text added: "R139"
- board text added: "R140"
- board text added: "R141"
- board text added: "R142"
- board text added: "R143"
- board text added: "R144"
- board text added: "R145"
- board text added: "R146"
- board text added: "R147"
- board text added: "R148"
- board text added: "R149"
- board text added: "R150"
- board text added: "R151"
- board text added: "R152"
- board text added: "R153"
- board text added: "R154"
- board text added: "R155"
- board text added: "R156"
- board text added: "R157"
- board text added: "R158"
- board text added: "R159"
- board text added: "RJ-45 Ethernet X18"
- board text added: "TP3"
- board text added: "TP4"
- board text added: "X12"
- board text added: "X13"
- board text added: "X14"
- board text added: "X15"
- board text added: "X16"
- board text added: "X17"
- board text added: "X18"
- board text added: "X19"
- board text added: "X20"
- board text added: "ZD10"
- board text added: "ZD11"
- board text added: "ZD12"
- board text added: "ZD8"
- board text added: "ZD9"
- board text removed: "8-pin WIFI connector"
- board text removed: "C1"
- board text removed: "C10"
- board text removed: "C11"
- board text removed: "C12"
- board text removed: "C13"
- board text removed: "C14"
- board text removed: "C15"
- board text removed: "C16"
- board text removed: "C17"
- board text removed: "C18"
- board text removed: "C19"
- board text removed: "C2"
- board text removed: "C20"
- board text removed: "C21"
- board text removed: "C22"
- board text removed: "C23"
- board text removed: "C24"
- board text removed: "C25"
- board text removed: "C26"
- board text removed: "C27"
- board text removed: "C28"
- board text removed: "C29"
- board text removed: "C3"
- board text removed: "C30"
- board text removed: "C31"
- board text removed: "C32"
- board text removed: "C33"
- board text removed: "C34"
- board text removed: "C35"
- board text removed: "C36"
- board text removed: "C37"
- board text removed: "C38"
- board text removed: "C39"
- board text removed: "C4"
- board text removed: "C40"
- board text removed: "C41"
- board text removed: "C42"
- board text removed: "C43"
- board text removed: "C44"
- board text removed: "C45"
- board text removed: "C46"
- board text removed: "C47"
- board text removed: "C48"
- board text removed: "C49"
- board text removed: "C5"
- board text removed: "C50"
- board text removed: "C51"
- board text removed: "C52"
- board text removed: "C53"
- board text removed: "C6"
- board text removed: "C7"
- board text removed: "C8"
- board text removed: "C9"
- board text removed: "Ch#1 control X1"
- board text removed: "Ch#2 control X3"
- board text removed: "D1"
- board text removed: "D2"
- board text removed: "D3"
- board text removed: "D4"
- board text removed: "D5"
- board text removed: "D6"
- board text removed: "D7"
- board text removed: "D8"
- board text removed: "Encoder X8"
- board text removed: "Ethernet module X9"
- board text removed: "FB"
- board text removed: "IC1"
- board text removed: "IC10"
- board text removed: "IC11"
- board text removed: "IC13"
- board text removed: "IC14"
- board text removed: "IC15"
- board text removed: "IC2"
- board text removed: "IC3"
- board text removed: "IC4"
- board text removed: "IC5"
- board text removed: "IC6"
- board text removed: "IC7"
- board text removed: "IC8"
- board text removed: "IC9"
- board text removed: "JP1"
- board text removed: "JP2"
- board text removed: "OK1"
- board text removed: "Power X5"
- board text removed: "Power module X2,X4"
- board text removed: "Q1"
- board text removed: "Q2"
- board text removed: "Q3"
- board text removed: "Q4"
- board text removed: "Q5"
- board text removed: "Q6"
- board text removed: "Q7"
- board text removed: "Q8"
- board text removed: "R1"
- board text removed: "R10"
- board text removed: "R11"
- board text removed: "R12"
- board text removed: "R13"
- board text removed: "R14"
- board text removed: "R15"
- board text removed: "R16"
- board text removed: "R17"
- board text removed: "R18"
- board text removed: "R19"
- board text removed: "R2"
- board text removed: "R20"
- board text removed: "R21"
- board text removed: "R22"
- board text removed: "R23"
- board text removed: "R24"
- board text removed: "R25"
- board text removed: "R26"
- board text removed: "R27"
- board text removed: "R28"
- board text removed: "R29"
- board text removed: "R3"
- board text removed: "R30"
- board text removed: "R31"
- board text removed: "R32"
- board text removed: "R33"
- board text removed: "R34"
- board text removed: "R35"
- board text removed: "R36"
- board text removed: "R37"
- board text removed: "R38"
- board text removed: "R4"
- board text removed: "R5"
- board text removed: "R6"
- board text removed: "R7"
- board text removed: "R8"
- board text removed: "R9"
- board text removed: "RJ-45 Ethernet X7"
- board text removed: "TP1"
- board text removed: "TP2"
- board text removed: "X1"
- board text removed: "X2"
- board text removed: "X3"
- board text removed: "X4"
- board text removed: "X5"
- board text removed: "X6"
- board text removed: "X7"
- board text removed: "X8"
- board text removed: "X9"
- board text removed: "ZD1"
- board text removed: "ZD2"
- board text removed: "ZD3"
- board text removed: "ZD4"
- board text removed: "ZD5"
